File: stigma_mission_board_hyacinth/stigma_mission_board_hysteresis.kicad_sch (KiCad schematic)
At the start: 149 parts, among them J1 DF40C-70DS-0.4V(51), J2 DF40HB(2.5)-10DS-0.4V(51), J7 SMA, J8 SMA, J9 JST-GH 4Pin, Q1 DMN2056U, U1 LAN8742A, U10 MCP2562-E-SN, U11 MCP2562-E-SN, U12 SN74HCS594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

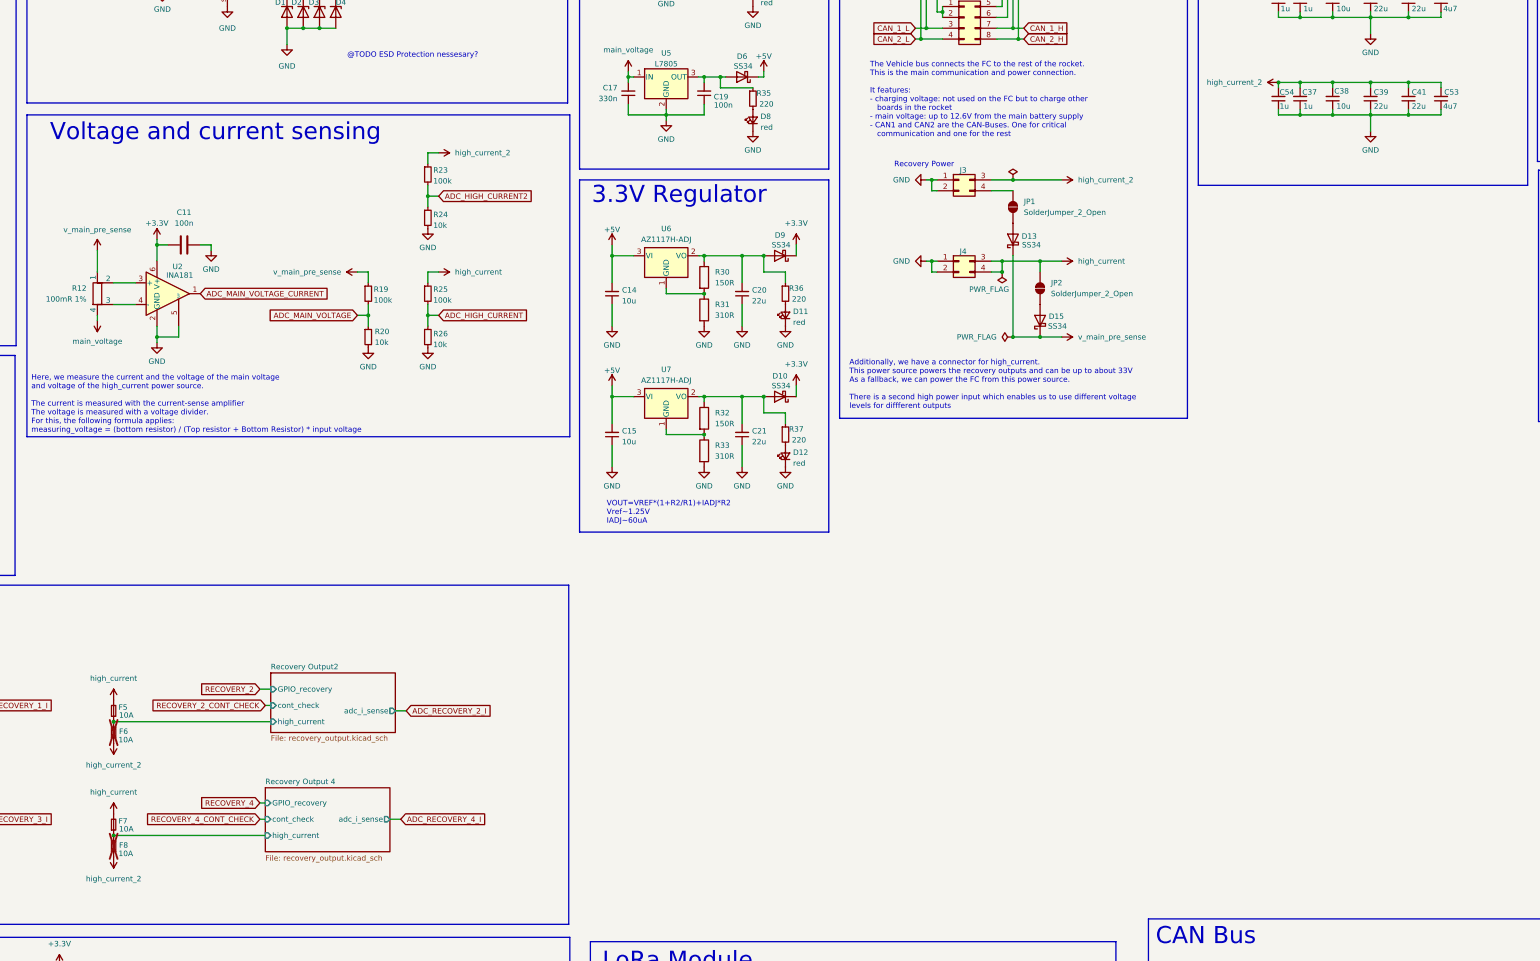
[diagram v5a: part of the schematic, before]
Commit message: Added more components to NEW pcb layout.
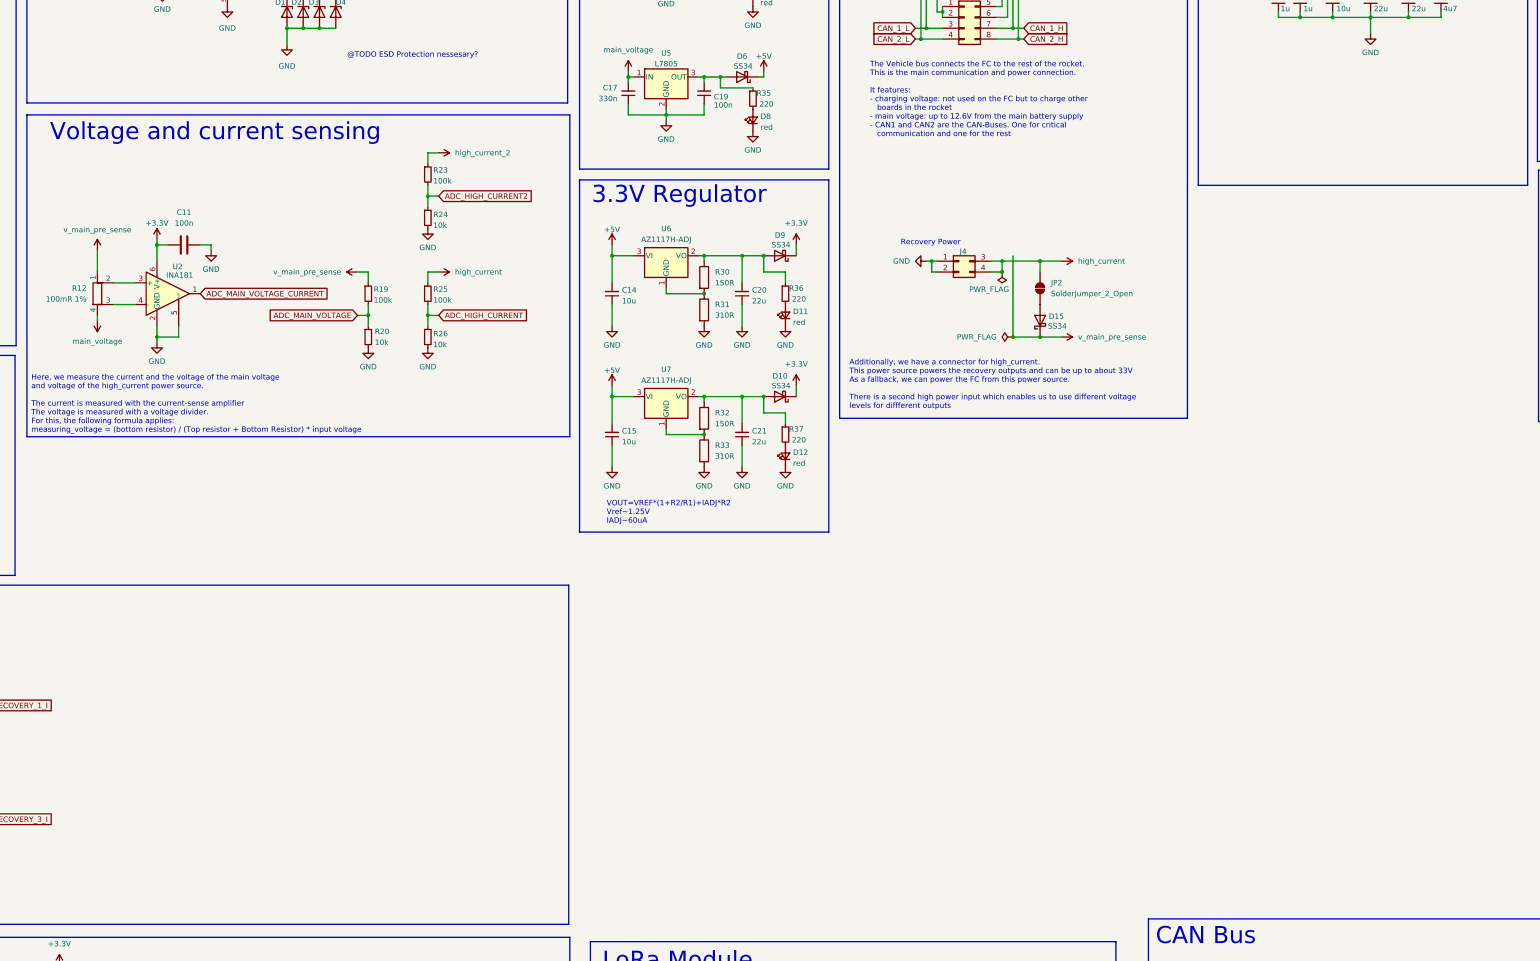
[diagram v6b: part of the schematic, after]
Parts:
- removed C37, C54: 1u, Capacitor_SMD:C_0603_1608Metric, symbol Device:C_Small
- removed C38: 10u, Capacitor_SMD:C_0805_2012Metric, symbol Device:C_Small
- removed C39, C41: 22u, Capacitor_SMD:C_0805_2012Metric, symbol Device:C_Small
- removed C53: 4u7, Capacitor_SMD:C_0805_2012Metric, symbol Device:C_Small
- removed D13: SS34, Diode_SMD:D_SMA, symbol Diode:SS34
- removed F5, F6, F7, F8: 10A, Fuse:Fuse_1206_3216Metric, symbol Device:Fuse_Small
- removed J3: ~, Connector_Molex:Molex_Micro-Fit_3.0_43045-0400_2x02_P3.00mm_Horizontal, symbol Connector_Generic:Conn_02x02_Top_Bottom
- removed JP1: SolderJumper_2_Open, Jumper:SolderJumper-2_P1.3mm_Open_Pad1.0x1.5mm, symbol Jumper:SolderJumper_2_Open
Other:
- removed sheet Recovery Output 4
- removed sheet Recovery Output2

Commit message: added some 3d models
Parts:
- J4: footprint Connector_Molex:Molex_Micro-Fit_3.0_43045-0400_2x02_P3.00mm_Horizontal -> stigma:Molex_Micro-Fit_3.0_43045-0400_2x02_P3.00mm_Horizontal
- J5, J6: footprint Connector_Molex:Molex_Micro-Fit_3.0_43045-0800_2x04_P3.00mm_Horizontal -> stigma:Molex_Micro-Fit_3.0_43045-0800_2x04_P3.00mm_Horizontal
- J7: footprint Connector_Coaxial:SMA_Amphenol_901-143_Horizontal -> stigma:SMA_Amphenol_901-143_Horizontal
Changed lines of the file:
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@@
 			)
 		)
-		(property "Footprint" "Connector_Coaxial:SMA_Amphenol_901-143_Horizontal"
+		(property "Footprint" "stigma:SMA_Amphenol_901-143_Horizontal"
 			(at 349.25 299.72 0)
 			(effects
@@
 			)
 		)
-		(property "Datasheet" " ~"
+		(property "Datasheet" "~"
 			(at 349.25 299.72 0)
 			(effects
@@
 			)
 		)
-		(property "Footprint" "Connector_Molex:Molex_Micro-Fit_3.0_43045-0800_2x04_P3.00mm_Horizontal"
+		(property "Footprint" "stigma:Molex_Micro-Fit_3.0_43045-0800_2x04_P3.00mm_Horizontal"
 			(at 336.55 40.64 0)
 			(effects
@@
 			)
 		)
-		(property "Datasheet" ""
+		(property "Datasheet" "https://www.molex.com/en-us/products/part-detail-pdf/430450800?display=pdf"
 			(at 336.55 40.64 0)
 			(effects
@@
 			)
 		)
-		(property "Description" ""
+		(property "Description" "43045-0800"
 			(at 336.55 40.64 0)
 			(effects
@@
 			)
 		)
-		(property "Footprint" "Connector_Molex:Molex_Micro-Fit_3.0_43045-0400_2x02_P3.00mm_Horizontal"
+		(property "Footprint" "stigma:Molex_Micro-Fit_3.0_43045-0400_2x02_P3.00mm_Horizontal"
 			(at 335.28 113.03 0)
 			(effects
@@
 			)
 		)
-		(property "Datasheet" ""
+		(property "Datasheet" "https://www.mouser.de/ProductDetail/Molex/43045-0400?qs=UeCeOHRHQeaIqmxE9Bxdrw%3D%3D#:~:text=Datenblatt%3A,43045%2D0400%20Datenblatt"
 			(at 335.28 113.03 0)
 			(effects
@@
 			)
 		)
-		(property "Description" ""
+		(property "Description" "43045-0400"
 			(at 335.28 113.03 0)
 			(effects
@@
 			)
 		)
-		(property "Footprint" "Connector_Molex:Molex_Micro-Fit_3.0_43045-0800_2x04_P3.00mm_Horizontal"
+		(property "Footprint" "stigma:Molex_Micro-Fit_3.0_43045-0800_2x04_P3.00mm_Horizontal"
 			(at 336.55 55.88 0)
 			(effects
@@
 			)
 		)
-		(property "Datasheet" ""
+		(property "Datasheet" "https://www.molex.com/en-us/products/part-detail-pdf/430450800?display=pdf"
 			(at 336.55 55.88 0)
 			(effects
@@
 			)
 		)
-		(property "Description" ""
+		(property "Description" "43045-0800"
 			(at 336.55 55.88 0)
 			(effects

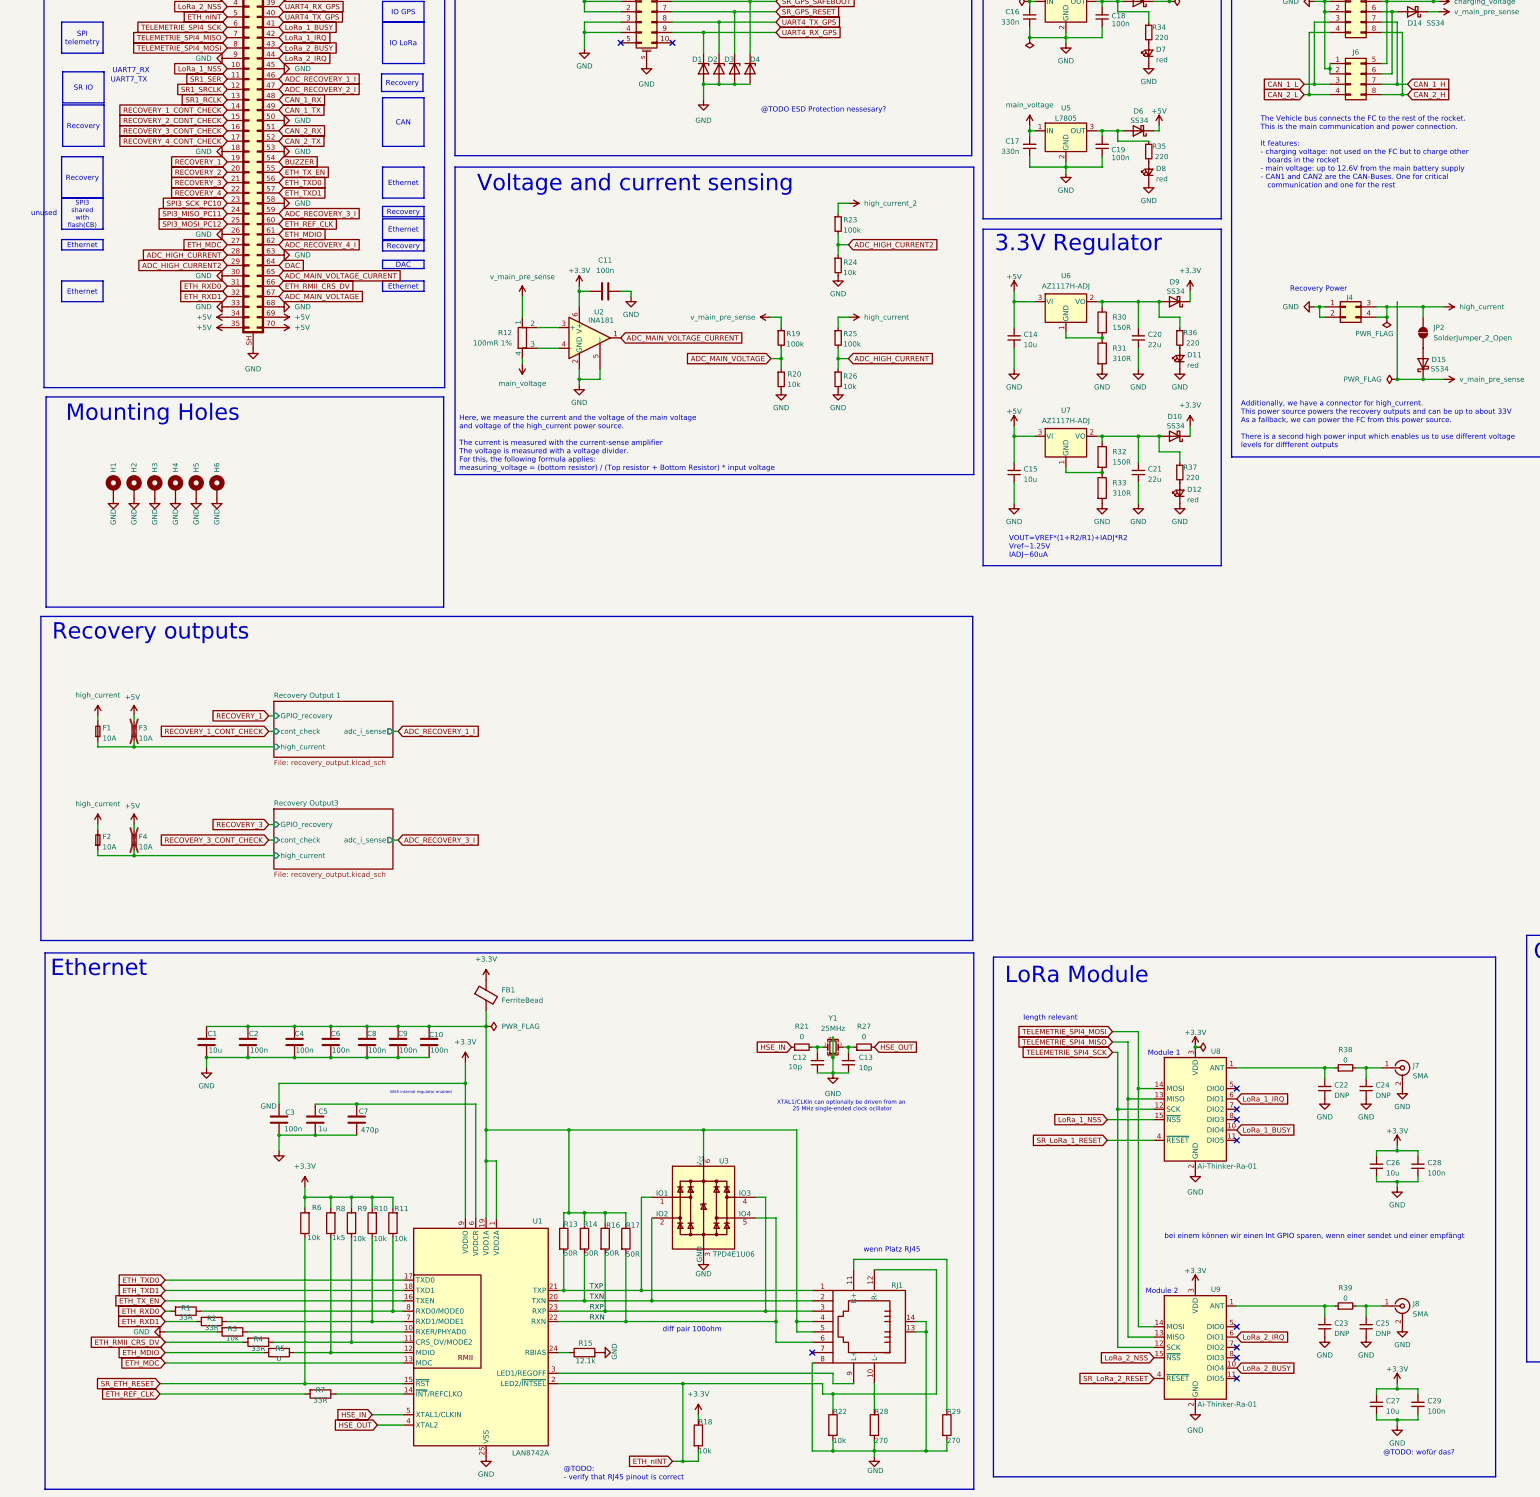
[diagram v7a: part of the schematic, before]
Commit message: Rework recovery outputs to 2x2 low side
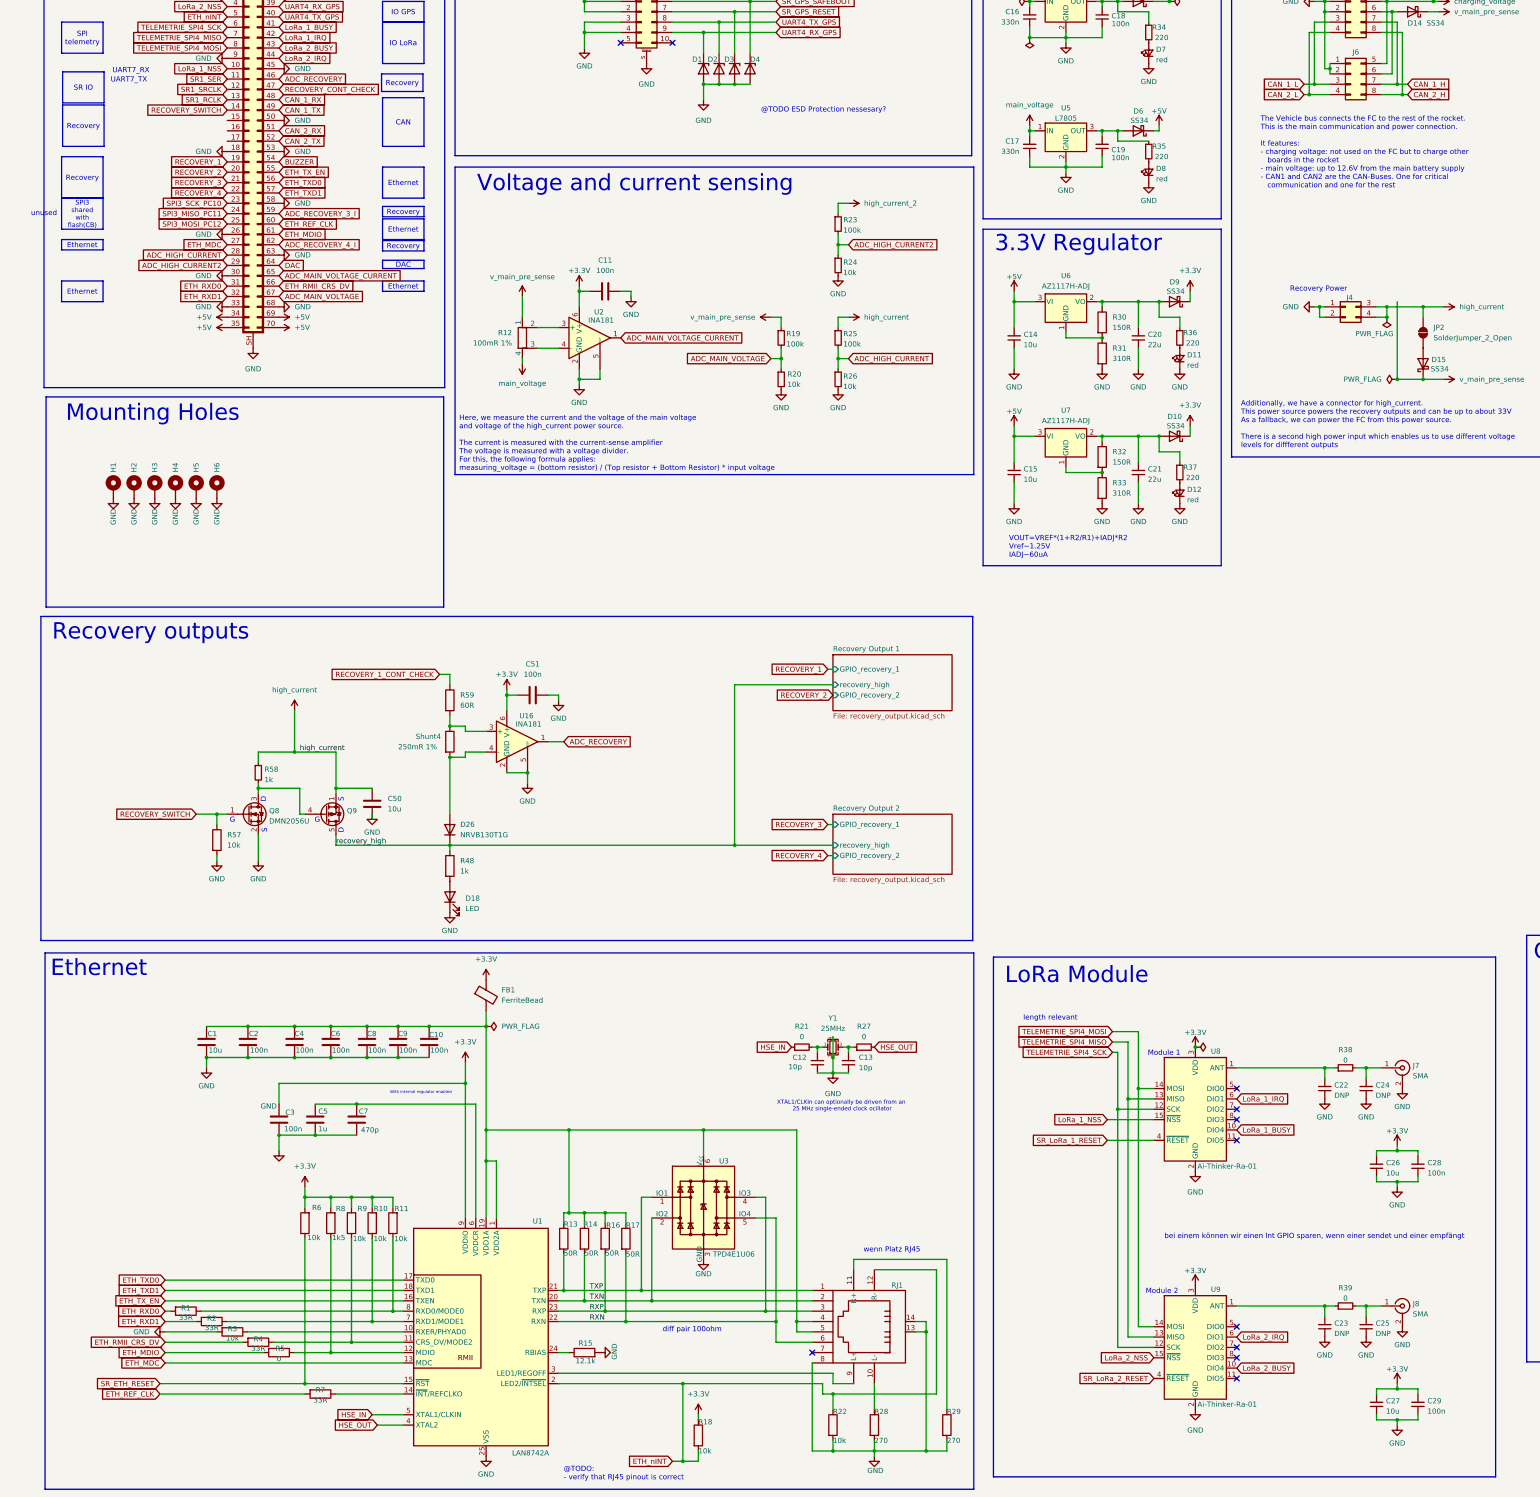
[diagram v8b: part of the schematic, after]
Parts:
- removed F1, F2, F3, F4: 10A, Fuse:Fuse_1206_3216Metric, symbol Device:Fuse_Small
- added C50: 10u, Capacitor_SMD:C_1206_3216Metric, symbol Device:C
- added C51: 100n, Capacitor_SMD:C_0603_1608Metric, symbol Device:C
- added D18: LED, LED_SMD:LED_0603_1608Metric, symbol Device:LED
- added D26: NRVB130T1G, Diode_SMD:D_SOD-123, symbol Device:D
- added Q8: DMN2056U, Package_TO_SOT_SMD:SOT-23, symbol Transistor_FET:DMG2302U
- added Q9: AOSP21321, Package_SO:SO-8_3.9x4.9mm_P1.27mm, symbol euroc_fc:AOSP21321
- added R48: 1k, Resistor_SMD:R_0603_1608Metric, symbol Device:R
- added R57: 10k, Resistor_SMD:R_0603_1608Metric, symbol Device:R
- added R58: 1k, Resistor_SMD:R_0603_1608Metric, symbol Device:R_Small
- added R59: 60R, Resistor_SMD:R_0603_1608Metric, symbol Device:R
- added Shunt4: 250mR 1%, Resistor_SMD:R_0805_2012Metric, symbol Device:R
- added U16: INA181, Package_TO_SOT_SMD:SOT-23-6, symbol Amplifier_Current:INA181
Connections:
- net +3.3V: now also C51.1, U16.6 (V+)
- net GND: now also C50.2, C51.2, D18.1 (K), Q8.2 (S), R57.2, U16.2 (GND), U16.5 (REF)
- net RECOVERY_1_CONT_CHECK: now also R59.1; no longer J1.14 (Pin_14)
- net high_current: now also C50.1, Q9.1 (S), Q9.2 (S), Q9.3 (S), R58.1
- net ADC_RECOVERY_1_I renamed ADC_RECOVERY
- net ADC_RECOVERY: now also U16.1
- net ADC_RECOVERY_2_I renamed RECOVERY_CONT_CHECK
- net RECOVERY_2_CONT_CHECK: no longer names the net of J1.15 (Pin_15)
- net RECOVERY_3_CONT_CHECK: no longer names the net of J1.16 (Pin_16)
- net RECOVERY_4_CONT_CHECK: no longer names the net of J1.17 (Pin_17)
- new net: Q8.3 (D), Q9.4 (G), R58.2
- new net: R59.2, Shunt4.1, U16.3 (+)
- new net: D26.2 (A), Shunt4.2, U16.4 (-)
- new net: D18.2 (A), R48.2
- new net RECOVERY_SWITCH: J1.14 (Pin_14), Q8.1 (G), R57.1
- new net recovery_high: D26.1 (K), Q9.5 (D), Q9.6 (D), Q9.7 (D), Q9.8 (D), R48.1
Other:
- sheet Recovery Output3 renamed Recovery Output 2
- sheet Recovery Output 1 ports: added GPIO_recovery_1, GPIO_recovery_2, recovery_high; removed GPIO_recovery, adc_i_sense, cont_check, high_current
- sheet Recovery Output 2 ports: added GPIO_recovery_1, GPIO_recovery_2, recovery_high; removed GPIO_recovery, adc_i_sense, cont_check, high_current
- note added: "D"
- note added: "G"
- note added: "S"
- note removed: "@TODO: wofür das?"
